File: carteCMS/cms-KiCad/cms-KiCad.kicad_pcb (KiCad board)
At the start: 2 copper layers, 100 x 100 mm, 40 parts, among them IC1 CD4093BM, J1 Conn_01x02, J2 Conn_01x16, J3 AVR-ISP-6, J4 HP, SW1 SW_SPDT, SW2 SW-MCIPTG23K-V, SW3 SW-MCIPTG23K-V, SW4 SW-MCIPTG23K-V, U1 LM358, U3 max7426cua+T, U6 ATmega8U2-A, Y2 Crystal

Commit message: partie ana faite
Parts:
- moved J2 74.9 mm to (200.7, 74.5), turned to -90 degrees
- moved TP1 71.8 mm to (158.5, 165.0)
- moved TP3 71.3 mm to (181.0, 165.0)
- moved C10 70.5 mm to (186.9, 158.0), turned to 90 degrees
- moved TP4 68.2 mm to (193.0, 165.0)
- moved SW3 67.6 mm to (214.5, 103.5)
- moved SW4 66.9 mm to (214.0, 110.0)
- moved TP2 66.0 mm to (177.0, 165.0)
- moved C11 65.0 mm to (156.4, 152.0), turned to 0 degrees
- moved C4 63.4 mm to (177.5, 149.7), turned to -90 degrees
- moved R6 61.7 mm to (157.5, 157.0)
- moved C2 61.2 mm to (145.0, 157.0)
- moved IC1 61.2 mm to (193.0, 153.0), turned to 180 degrees
- moved R3 61.2 mm to (148.5, 157.0)
- moved U3 61.0 mm to (171.5, 153.2)
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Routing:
- net +5V: track 0.00 -> 141.9 mm
- net Net-(IC1-G): track 0.00 -> 28.6 mm
- net Net-(U3-IN): track 0.00 -> 27.0 mm
- net Net-(MK1-+): track 0.00 -> 17.5 mm
- net /Analog/100xFc: track 0.00 -> 15.6 mm, vias 0 -> 1
- net Net-(U3-COM): track 0.00 -> 15.0 mm
- net /Analog/Fmesure: track 0.00 -> 14.6 mm
- net Net-(J1-Pin_2): track 0.00 -> 13.6 mm
- net Net-(U1--): track 0.00 -> 11.8 mm
- net Net-(U1-+): track 0.00 -> 7.26 mm
- net Net-(U6-XTAL1): track 0.00 -> 5.17 mm
- net Net-(U6-PC0/XTAL2): track 0.00 -> 5.05 mm
- net Net-(C2-Pad2): track 0.00 -> 1.64 mm
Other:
- board text added: "Amplification"
- board text added: "Filtrage"
- board text added: "Mise en forme"

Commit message: partie num p1 - orga
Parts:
- moved C8 67.1 mm to (162.5, 83.5), turned to 90 degrees
- moved J2 62.0 mm to (212.1, 135.5)
- moved C6 57.7 mm to (176.5, 77.0), turned to 90 degrees
- moved R9 52.8 mm to (185.0, 91.8), turned to 180 degrees
- moved C3 42.2 mm to (190.3, 88.0)
- moved J4 42.2 mm to (204.2, 91.5), turned to 90 degrees
- moved SW2 41.3 mm to (186.0, 95.2), turned to 0 degrees
- moved Y2 38.0 mm to (185.3, 83.0)
- moved U6 37.6 mm to (176.0, 84.2), turned to -90 degrees
- moved C7 34.8 mm to (181.5, 95.2), turned to -90 degrees
- moved C5 34.2 mm to (190.3, 78.0)
- moved R8 23.6 mm to (219.5, 111.0), turned to 180 degrees
- moved J3 22.8 mm to (160.0, 87.5), turned to 0 degrees
- moved SW3 21.6 mm to (219.5, 124.5)
- moved R7 18.4 mm to (219.5, 113.5), turned to 180 degrees
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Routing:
- net RS: track 0.00 -> 85.7 mm
- net R/W: track 0.00 -> 82.0 mm
- net E: track 0.00 -> 78.3 mm
- net Net-(J2-Pin_7): track 0.00 -> 73.6 mm
- net Net-(J2-Pin_8): track 0.00 -> 69.9 mm
- net Net-(J2-Pin_9): track 0.00 -> 65.2 mm
- net Net-(J2-Pin_10): track 0.00 -> 49.3 mm
- net Net-(J2-Pin_11): track 0.00 -> 45.0 mm
- net Net-(J2-Pin_12): track 0.00 -> 41.5 mm
- net Net-(J2-Pin_13): track 0.00 -> 38.1 mm
- net Net-(J2-Pin_14): track 0.00 -> 34.6 mm
- net +5V: track 141.9 -> 126.6 mm
- net Net-(U6-XTAL1): track 5.17 -> 15.1 mm
- net Net-(U6-PC0/XTAL2): track 5.05 -> 14.6 mm
- net INT1/PD1: track 0.00 -> 6.38 mm
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
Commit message: partie num p2 - début cablage et amélioration orga
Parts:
- moved J4 14.1 mm to (215.2, 82.8), turned to 180 degrees
- moved C3 10.7 mm to (200.8, 85.8)
- moved C5 10.7 mm to (200.8, 75.8)
- moved C6 10.7 mm to (187.0, 74.8)
- moved C7 10.7 mm to (192.0, 93.0)
- moved R9 10.7 mm to (195.5, 89.5)
- moved SW2 10.7 mm to (196.5, 93.0)
- moved U6 10.7 mm to (186.5, 82.0)
- moved Y2 10.7 mm to (195.8, 80.8)
- moved C8 8.27 mm to (163.3, 75.3)
- moved J3 8.27 mm to (160.7, 79.2)
- moved SW3 6.25 mm to (219.5, 118.2)
- moved SW4 3.50 mm to (219.5, 124.0)
- turned R7 to 0 degrees
- turned R8 to 0 degrees
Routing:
- net INT2/PD2: track 3.41 -> 96.0 mm
- net INT1/PD1: track 6.38 -> 83.2 mm
- net Net-(J4-Pin_1): track 0.00 -> 40.2 mm
- net +5V: track 126.6 -> 144.3 mm
- net RESET: track 0.00 -> 14.5 mm
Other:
- board text added: "LCD"

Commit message: rework pcb : bientôt terminé
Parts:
- moved J2 86.0 mm to (129.0, 157.8), turned to 90 degrees
- moved TP2 71.8 mm to (166.5, 94.0)
- moved C11 56.0 mm to (149.0, 96.5)
- moved J3 55.3 mm to (206.5, 110.3), turned to 90 degrees
- moved TP4 54.7 mm to (180.3, 111.8)
- moved TP3 54.6 mm to (168.1, 112.0)
- moved TP1 53.6 mm to (152.5, 111.7)
- moved C10 52.3 mm to (174.2, 107.3)
- moved IC1 52.3 mm to (180.3, 102.3)
- moved C9 51.4 mm to (157.0, 105.2)
- moved U3 51.4 mm to (161.5, 102.7)
- moved MK1 51.2 mm to (132.2, 103.8)
- moved R2 51.2 mm to (134.1, 96.8)
- moved C8 51.1 mm to (202.8, 107.8), turned to 180 degrees
- moved C2 51.1 mm to (138.5, 106.2)
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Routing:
- net +5V: track 144.3 -> 356.1 mm, vias 0 -> 5
- net (no net): track 0.00 -> 136.5 mm
- net Net-(J2-Pin_14): track 34.6 -> 120.2 mm
- net Net-(J2-Pin_13): track 38.1 -> 120.3 mm
- net Net-(J2-Pin_12): track 41.5 -> 121.1 mm
- net Net-(J2-Pin_11): track 45.0 -> 121.2 mm
- net Net-(J2-Pin_10): track 49.3 -> 103.5 mm
- net Net-(J2-Pin_9): track 65.2 -> 102.2 mm
- net Net-(J2-Pin_8): track 69.9 -> 101.5 mm
- net RESET: track 14.5 -> 45.2 mm, vias 0 -> 1
- net /Analog/Fmesure: track 14.6 -> 40.1 mm
- net Net-(J4-Pin_1): track 40.2 -> 14.8 mm
- net /Analog/100xFc: track 15.6 -> 39.0 mm, vias 1 -> 0
- net INT2/PD2: track 96.0 -> 75.8 mm, vias 0 -> 2
- net Net-(J2-Pin_7): track 73.6 -> 89.9 mm
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- added copper zone on B.Cu, net GND
- added copper zone on F.Cu, net GND

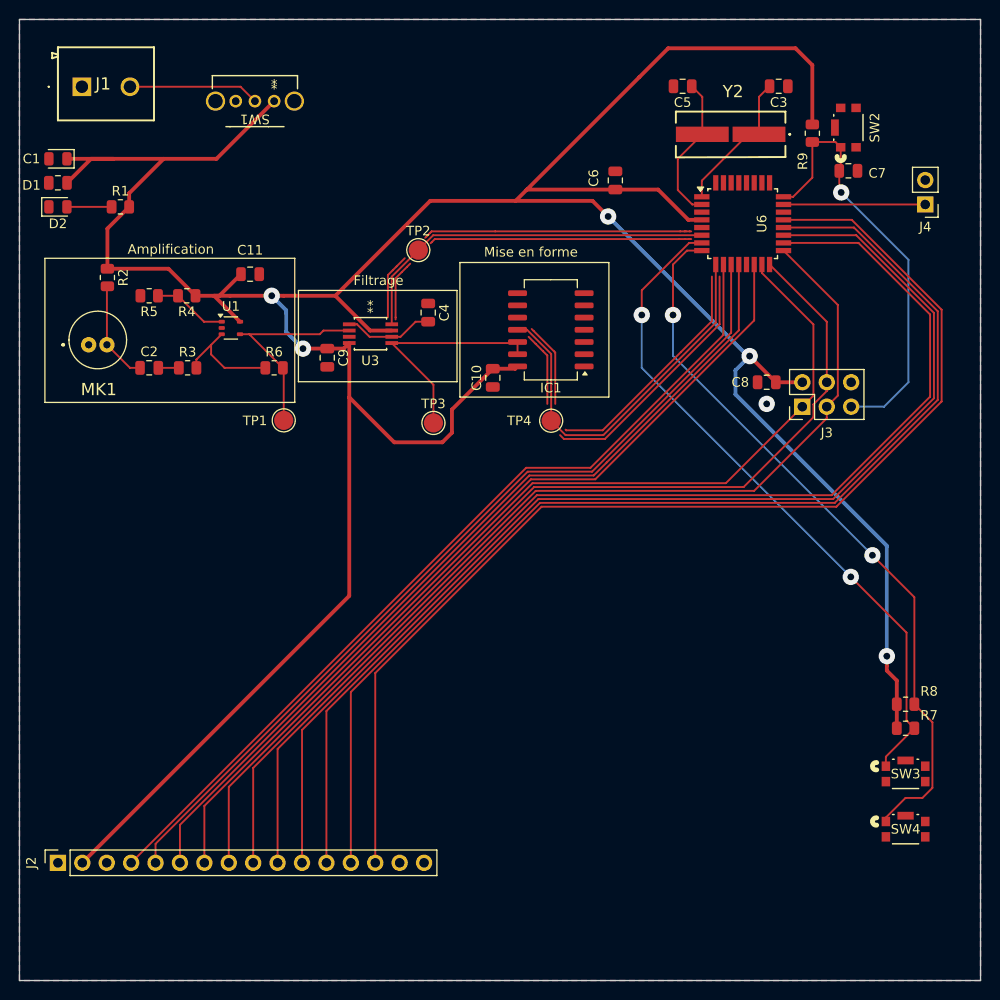
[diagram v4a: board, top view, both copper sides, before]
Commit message: projet final
schéma, routage, librairies et fichiers de fabrication
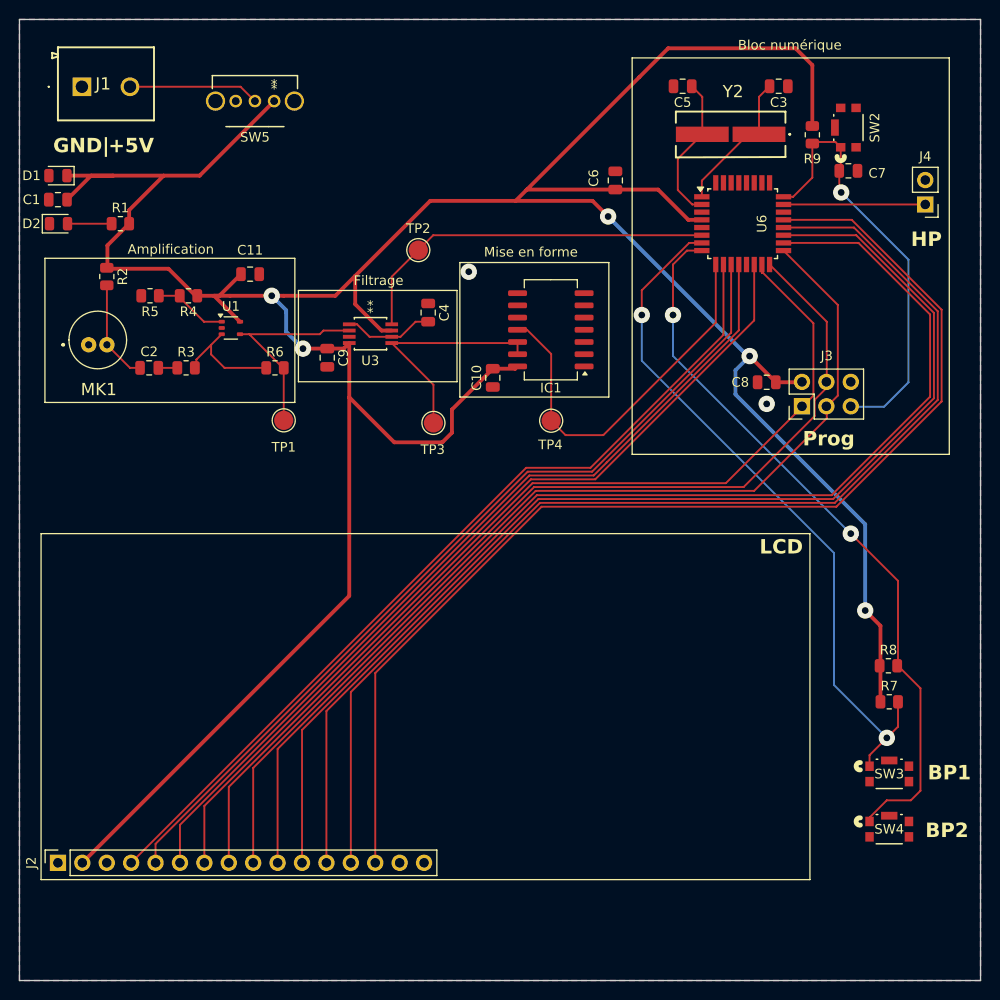
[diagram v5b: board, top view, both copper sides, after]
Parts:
- removed SW1: SW_SPDT, accordeurEmp:SWITCH_11MA1QS1
- added SW5: SW_SPDT, accordeurEmp:SWITCH_11MA1QS1, F.Cu at (151.5, 78.5)
- moved R8 4.38 mm to (215.4, 137.2)
- moved R7 3.23 mm to (215.5, 141.0)
- moved D2 1.75 mm to (129.1, 91.2)
- moved C1 1.75 mm to (129.0, 88.8)
- moved D1 1.75 mm to (129.0, 86.2)
- moved R1 1.75 mm to (135.5, 91.2)
- moved SW3 1.70 mm to (215.5, 148.5)
- moved SW4 1.70 mm to (215.5, 154.2)
- moved R4 0.18 mm to (142.6, 98.8)
- moved R9 0.16 mm to (207.5, 82.0)
- moved R3 0.16 mm to (142.3, 106.2)
- moved R2 0.12 mm to (134.1, 96.8)
- moved R5 0.09 mm to (138.6, 98.8)
- moved R6 0.09 mm to (151.6, 106.2)
- moved J3 0.06 mm to (206.4, 110.2)
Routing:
- net (no net): track 136.5 -> 0.00 mm
- net +5V: track 356.1 -> 351.7 mm
- net INT1/PD1: track 70.8 -> 73.6 mm
- net GND: vias 1 -> 2
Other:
- board text added: "+5V"
- board text added: "BP1"
- board text added: "BP2"
- board text added: "Bloc numérique"
- board text added: "GND|"
- board text added: "HP"
- board text added: "Prog"
